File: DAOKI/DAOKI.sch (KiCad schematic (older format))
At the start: 14 parts, among them CON4 CON4, U1 MOCH22a1, U2 LM393

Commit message: adding PCB
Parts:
- D2: footprint Resistor_SMD:R_0603_1608Metric_Pad0.98x0.95mm_HandSolder -> LED_SMD:LED_0603_1608Metric_Pad1.05x0.95mm_HandSolder
- R4: value 1K -> 100
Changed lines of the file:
@@
 P 6000 2150
 F 0 "R4" H 6070 2196 50  0000 L CNN
-F 1 "1K" H 6070 2105 50  0000 L CNN
+F 1 "100" H 6070 2105 50  0000 L CNN
 F 2 "Resistor_SMD:R_0603_1608Metric_Pad0.98x0.95mm_HandSolder" V 5930 2150 50  0001 C CNN
 F 3 "~" H 6000 2150 50  0001 C CNN
@@
 F 0 "D2" V 8539 1782 50  0000 R CNN
 F 1 "SWITCH INDICATION" V 8448 1782 50  0000 R CNN
-F 2 "Resistor_SMD:R_0603_1608Metric_Pad0.98x0.95mm_HandSolder" H 8500 1900 50  0001 C CNN
+F 2 "LED_SMD:LED_0603_1608Metric_Pad1.05x0.95mm_HandSolder" H 8500 1900 50  0001 C CNN
 F 3 "~" H 8500 1900 50  0001 C CNN
 	1    8500 1900

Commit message: New routing
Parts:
- D1, D2: footprint LED_SMD:LED_0603_1608Metric_Pad1.05x0.95mm_HandSolder -> LED_SMD:LED_1206_3216Metric_Castellated
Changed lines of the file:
@@
 F 0 "D1" V 4639 1982 50  0000 R CNN
 F 1 "POWER INDICATION" V 4548 1982 50  0000 R CNN
-F 2 "LED_SMD:LED_0603_1608Metric_Pad1.05x0.95mm_HandSolder" H 4600 2100 50  0001 C CNN
+F 2 "LED_SMD:LED_1206_3216Metric_Castellated" H 4600 2100 50  0001 C CNN
 F 3 "~" H 4600 2100 50  0001 C CNN
 	1    4600 2100
@@
 F 0 "D2" V 8539 1782 50  0000 R CNN
 F 1 "SWITCH INDICATION" V 8448 1782 50  0000 R CNN
-F 2 "LED_SMD:LED_0603_1608Metric_Pad1.05x0.95mm_HandSolder" H 8500 1900 50  0001 C CNN
+F 2 "LED_SMD:LED_1206_3216Metric_Castellated" H 8500 1900 50  0001 C CNN
 F 3 "~" H 8500 1900 50  0001 C CNN
 	1    8500 1900

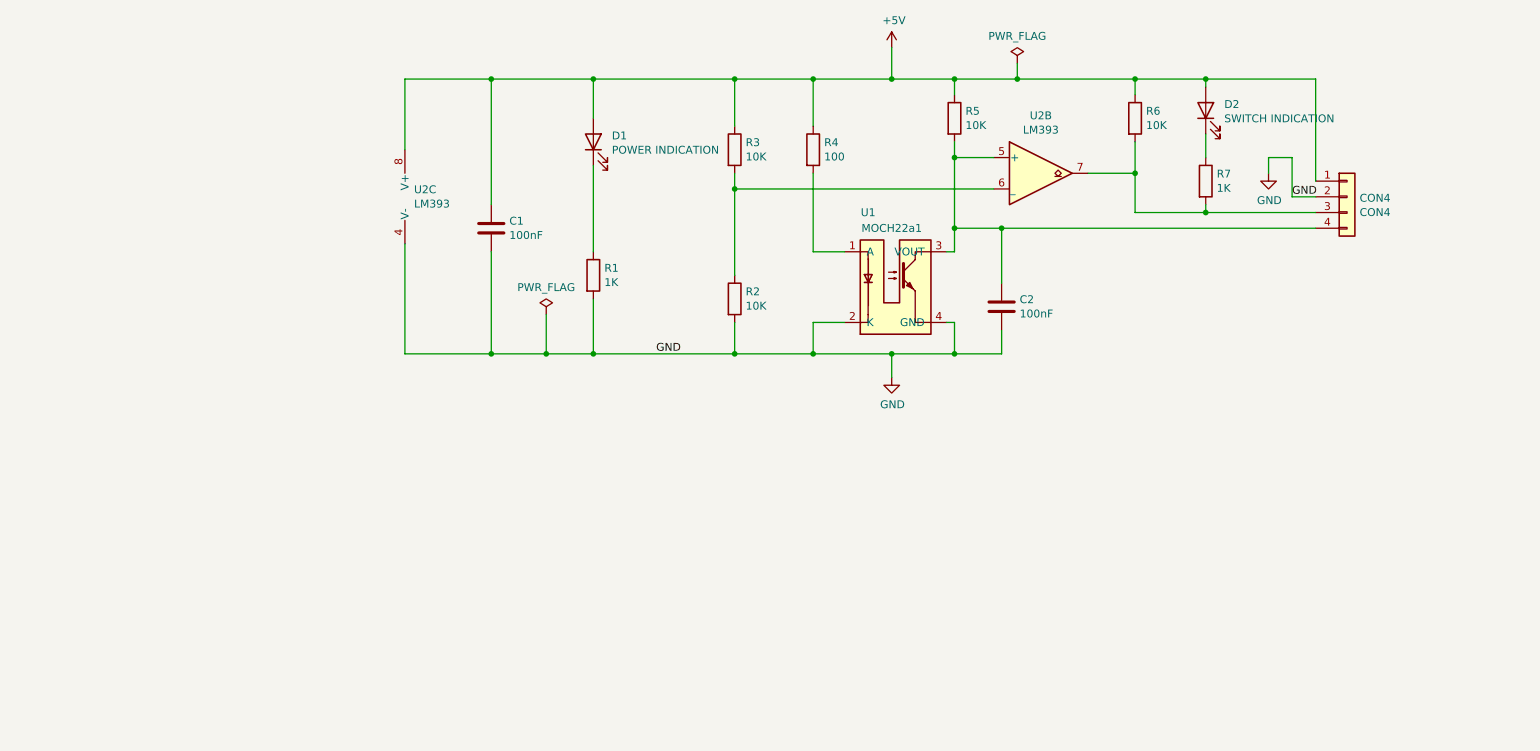
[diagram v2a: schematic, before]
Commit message: Some schematic improvements
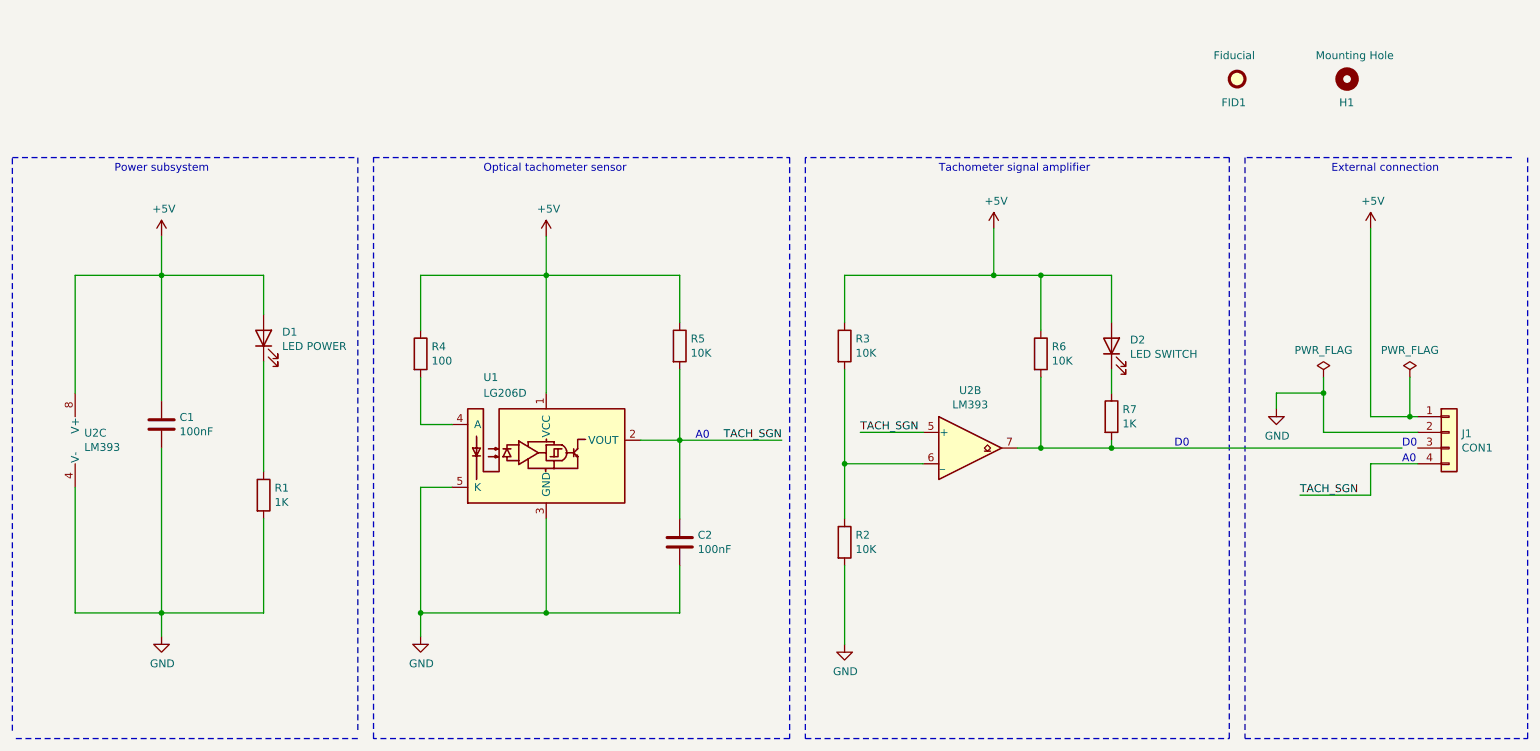
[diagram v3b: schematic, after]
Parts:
- removed U1: MOCH22a1, DAOKI:DIPS254W40P760L2450H1110Q4N, symbol DAOKI:MOCH22a1
- added FID1: Fiducial, Fiducial:Fiducial_1mm_Mask2mm, symbol Mechanical:Fiducial
- added H1: Mounting Hole, MountingHole:MountingHole_4.3mm_M4, symbol Mechanical:MountingHole
- added U1: LG206D, OptoDevice:Kodenshi_LG206D, symbol Sensor_Proximity:LG206D
- C1, C2: footprint Capacitor_SMD:C_0603_1608Metric_Pad1.08x0.95mm_HandSolder -> Capacitor_SMD:C_0805_2012Metric_Pad1.18x1.45mm_HandSolder
- D1: value POWER INDICATION -> LED POWER
- D2: value SWITCH INDICATION -> LED SWITCH
- J1: renamed from CON4; value CON4 -> CON1
- R1, R2, R3, R4, R5, R6, R7: footprint Resistor_SMD:R_0603_1608Metric_Pad0.98x0.95mm_HandSolder -> Resistor_SMD:R_0805_2012Metric_Pad1.20x1.40mm_HandSolder
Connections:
- net +5V: now also U1.1 (VCC)
- net GND: now also U1.3 (GND), U1.5 (K)
- net at R4.2: now also U1.4 (A)
- net TACH_SGN: now reaches C2.1, J1.4 (Pin_4), R5.2, U2.5 (+)
- net TACH_SGN: now also U1.2 (VOUT)
- net at R6.2, R7.2, U2.7: no longer J1.3 (Pin_3)
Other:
- note added: "A0"
- note added: "A0\n"
- note added: "D0"
- note added: "D0\n"
- note added: "External connection"
- note added: "Optical tachometer sensor"
- note added: "Power subsystem"
- note added: "Tachometer signal amplifier"
- moved on the sheet: C1, C2, D1, D2, J1, R1, R2, R3, R4, R5, R6, R7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
